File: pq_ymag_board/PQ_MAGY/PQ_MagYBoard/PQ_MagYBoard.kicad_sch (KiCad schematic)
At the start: 14 parts, among them J1 M20-7810245

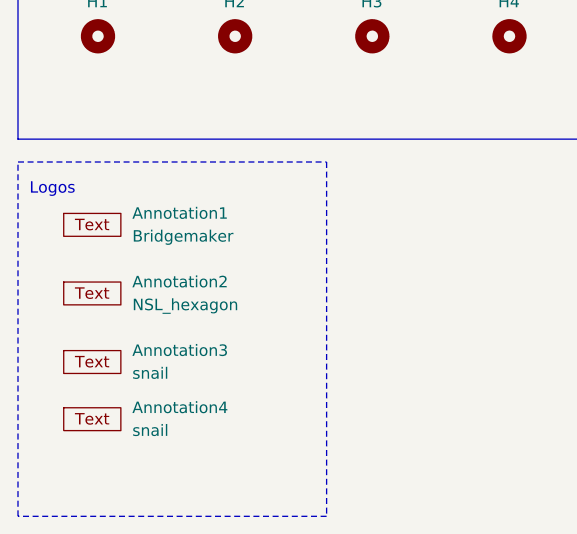
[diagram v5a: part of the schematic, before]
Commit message: add missing component names and relocate others
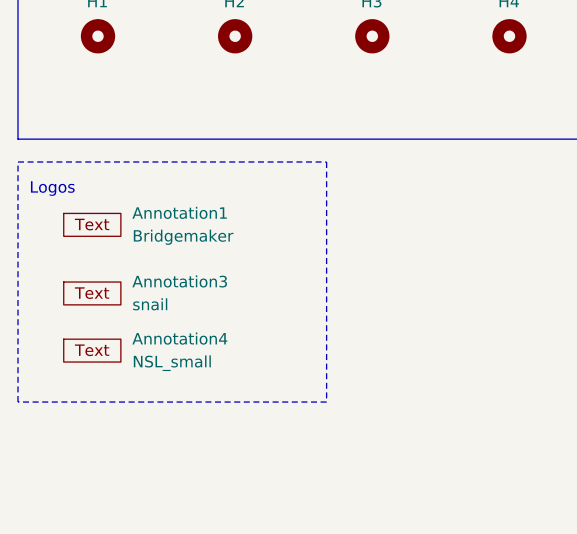
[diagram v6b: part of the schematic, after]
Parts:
- removed Annotation2: NSL_hexagon, symbols-nsl:NSL_hexagon, symbol symbols-nsl:Silkscreen_Annotation
- Annotation4: value snail -> NSL_small; footprint symbols-nsl:pocat_lektron -> symbols-nsl:NSL-small
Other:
- moved on the sheet: Annotation3, Annotation4
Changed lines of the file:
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@@
     (stroke (width 0) (type default))
   )
-  (rectangle (start 87.63 125.73) (end 121.92 165.1)
+  (rectangle (start 87.63 125.73) (end 121.92 152.4)
     (stroke (width 0) (type dash))
     (fill (type none))
@@
     )
   )
-  (symbol (lib_id "-nsl_symbols:Silkscreen_Annotation") (at 93.98 160.02 0) (unit 1)
+  (symbol (lib_id "-nsl_symbols:Silkscreen_Annotation") (at 93.98 152.4 0) (unit 1)
     (in_bom yes) (on_board yes) (dnp no) (fields_autoplaced)
-    (property "Reference" "Annotation4" (at 100.33 153.035 0)
+    (property "Reference" "Annotation4" (at 100.33 145.415 0)
       (effects (font (size 1.27 1.27)) (justify left))
     )
-    (property "Value" "snail" (at 100.33 155.575 0)
+    (property "Value" "NSL_small" (at 100.33 147.955 0)
       (effects (font (size 1.27 1.27)) (justify left))
     )
-    (property "Footprint" "symbols-nsl:pocat_lektron" (at 93.98 160.02 0)
+    (property "Footprint" "symbols-nsl:NSL-small" (at 93.98 152.4 0)
       (effects (font (size 1.27 1.27)) hide)
     )
-    (property "Datasheet" "" (at 93.98 160.02 0)
+    (property "Datasheet" "" (at 93.98 152.4 0)
       (effects (font (size 1.27 1.27)) hide)
     )
@@
     )
   )
-  (symbol (lib_id "-nsl_symbols:Silkscreen_Annotation") (at 93.98 153.67 0) (unit 1)
+  (symbol (lib_id "-nsl_symbols:Silkscreen_Annotation") (at 93.98 146.05 0) (unit 1)
     (in_bom yes) (on_board yes) (dnp no) (fields_autoplaced)
-    (property "Reference" "Annotation3" (at 100.33 146.685 0)
+    (property "Reference" "Annotation3" (at 100.33 139.065 0)
       (effects (font (size 1.27 1.27)) (justify left))
     )
-    (property "Value" "snail" (at 100.33 149.225 0)
+    (property "Value" "snail" (at 100.33 141.605 0)
       (effects (font (size 1.27 1.27)) (justify left))
     )
-    (property "Footprint" "symbols-nsl:Snail" (at 93.98 153.67 0)
+    (property "Footprint" "symbols-nsl:Snail" (at 93.98 146.05 0)
       (effects (font (size 1.27 1.27)) hide)
     )
-    (property "Datasheet" "" (at 93.98 153.67 0)
+    (property "Datasheet" "" (at 93.98 146.05 0)
       (effects (font (size 1.27 1.27)) hide)
     )
@@
         )
       )
-    )
-  )
-  (symbol (lib_id "symbols-nsl:Silkscreen_Annotation") (at 93.98 146.05 0) (unit 1)
-    (in_bom yes) (on_board yes) (dnp no) (fields_autoplaced)
-    (property "Reference" "Annotation2" (at 100.33 139.065 0)
-      (effects (font (size 1.27 1.27)) (justify left))
-    )
-    (property "Value" "NSL_hexagon" (at 100.33 141.605 0)
-      (effects (font (size 1.27 1.27)) (justify left))
-    )
-    (property "Footprint" "symbols-nsl:NSL_hexagon" (at 93.98 146.05 0)
-      (effects (font (size 1.27 1.27)) hide)
-    )
-    (property "Datasheet" "" (at 93.98 146.05 0)
-      (effects (font (size 1.27 1.27)) hide)
-    )
-    (instances
-      (project "PQ_MagYBoard"
-        (path "/69ef6fcb-01e8-4c0b-998b-22cdfd5dc558"
-          (reference "Annotation2") (unit 1)
-        )
-      )
